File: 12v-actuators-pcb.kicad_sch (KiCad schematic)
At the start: 46 parts, among them J1 EV_1, J10 690367280676, J11 3.5mm WR-TBL, J2 EV_2, J3 EV_3, J4 PURGE, J5 MOTOR_15_1, J6 MOTOR_15_2, J7 MOTOR_15_3, J8 MOTOR_35_1, J9 MOTOR_35_2, Q1 SUM110P06-08L, Q2 2N7002, Q3 2N7002, Q4 G2302, Q5 G2302, Q6 G2302, Q7 G2302, U1 NUCLEO-F042K6, U2 WSEN-PDUS, X1 ESC_Emax_Bullet_15A, X2 ESC_Emax_Bullet_15A, X3 ESC_Emax_Bullet_15A, X4 ESC_Emax_Bullet_35A, X5 ESC_Emax_Bullet_35A

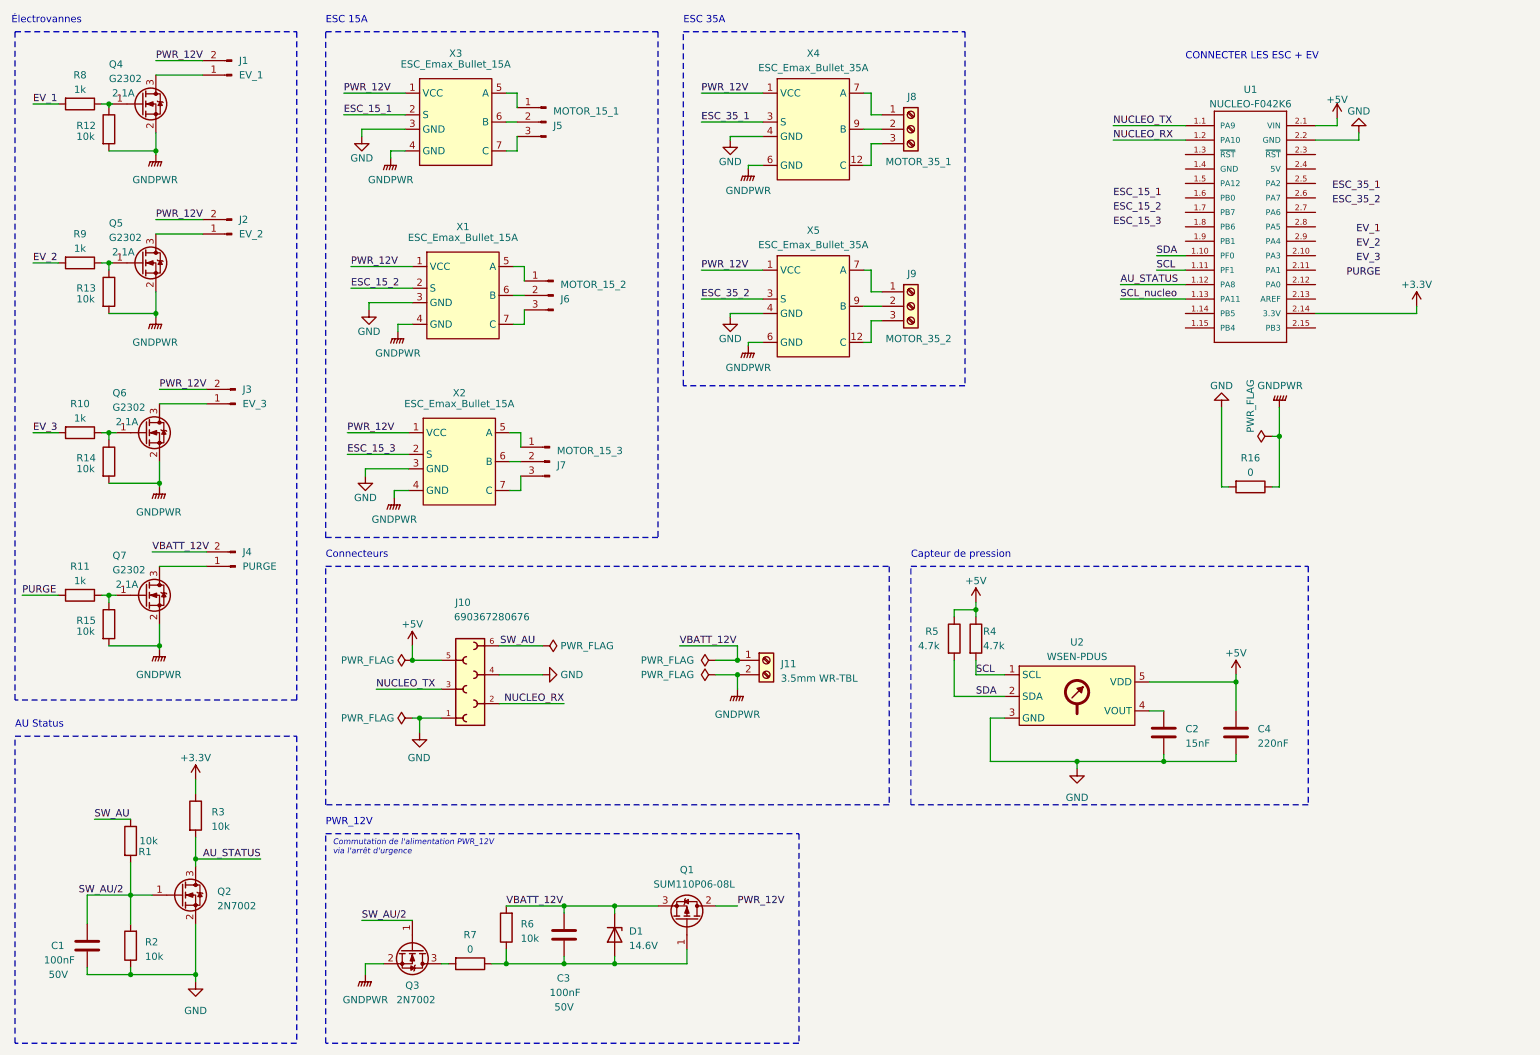
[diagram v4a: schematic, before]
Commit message: Reorganize and finish schematic, assign footprints
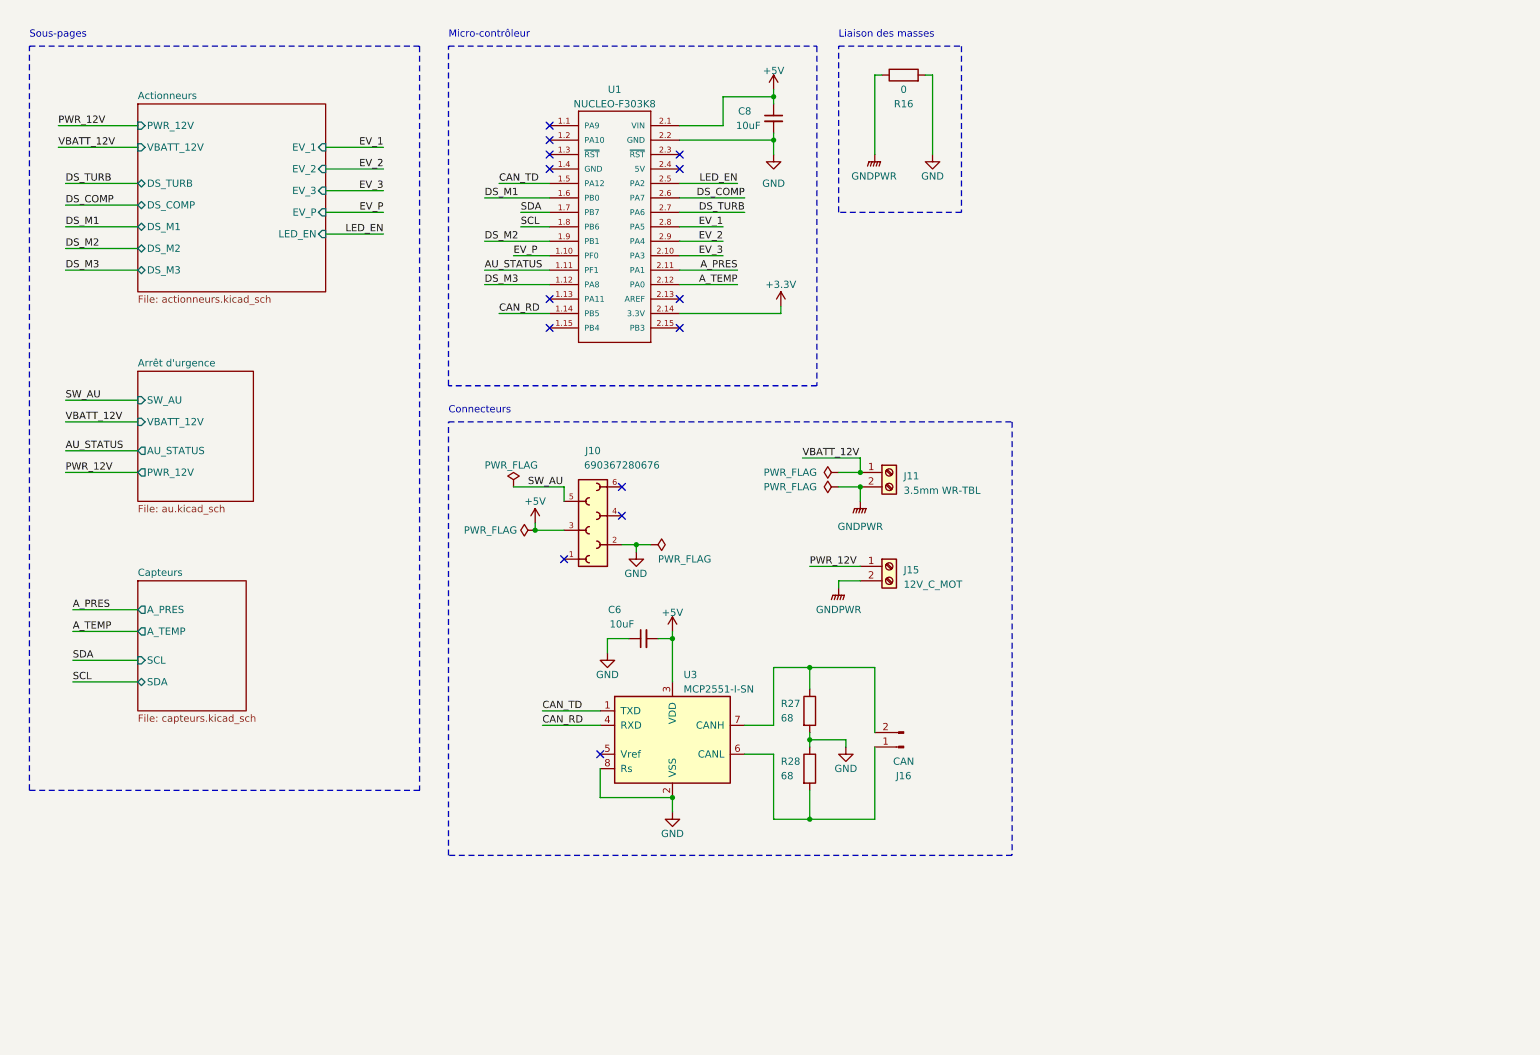
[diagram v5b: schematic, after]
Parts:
- removed C1, C3: 100nF, symbol Device:C
- removed C2: 15nF, symbol Device:C
- removed C4: 220nF, symbol Device:C
- removed D1: 14.6V, symbol Device:D_Zener
- removed J1: EV_1, symbol Connector:Conn_01x02_Pin
- removed J2: EV_2, symbol Connector:Conn_01x02_Pin
- removed J3: EV_3, symbol Connector:Conn_01x02_Pin
- removed J4: PURGE, symbol Connector:Conn_01x02_Pin
- removed J5: MOTOR_15_1, symbol Connector:Conn_01x03_Pin
- removed J6: MOTOR_15_2, symbol Connector:Conn_01x03_Pin
- removed J7: MOTOR_15_3, symbol Connector:Conn_01x03_Pin
- removed J8: MOTOR_35_1, symbol Connector:Screw_Terminal_01x03
- removed J9: MOTOR_35_2, symbol Connector:Screw_Terminal_01x03
- removed Q1: SUM110P06-08L, Package_TO_SOT_SMD:TO-252-2, symbol Transistor_FET:QM6015D
- removed Q2, Q3: 2N7002, Package_TO_SOT_SMD:SOT-23, symbol Transistor_FET:2N7002
- removed Q4, Q5, Q6, Q7: G2302, symbol Device:Q_NMOS_GSD
- removed R1, R2, R3, R6: 10k, Resistor_SMD:R_0201_0603Metric, symbol Device:R
- removed R10, R11, R8, R9: 1k, symbol Device:R
- removed R12, R13, R14, R15: 10k, symbol Device:R
- removed R4, R5: 4.7k, symbol Device:R
- removed R7: 0, Resistor_SMD:R_0201_0603Metric, symbol Device:R
- removed U2: WSEN-PDUS, symbol ComponentsEvo:WSEN-PDUS
- removed X1, X2, X3: ESC_Emax_Bullet_15A, ComponentsEvo:ESC_Emax_Bullet_15A, symbol ComponentsEvo:ESC_Emax_Bullet_15A
- removed X4, X5: ESC_Emax_Bullet_35A, ComponentsEvo:ESC_Emax_Bullet_35A, symbol ComponentsEvo:ESC_Emax_Bullet_35A
- added C6, C8: 10uF, Capacitor_SMD:C_0805_2012Metric, symbol Device:C_Small
- added J15: 12V_C_MOT, ConnectorsEvo:691321100002, symbol Connector:Screw_Terminal_01x02
- added J16: CAN, Connector_PinHeader_2.54mm:PinHeader_1x02_P2.54mm_Vertical, symbol Connector:Conn_01x02_Pin
- added R27, R28: 68, Resistor_SMD:R_0603_1608Metric, symbol Device:R
- added U3: MCP2551-I-SN, Package_SO:SOIC-8_3.9x4.9mm_P1.27mm, symbol Interface_CAN_LIN:MCP2551-I-SN
- J11: footprint (none) -> ConnectorsEvo:691321100002
- R16: footprint (none) -> Resistor_SMD:R_0805_2012Metric
- U1: value NUCLEO-F042K6 -> NUCLEO-F303K8
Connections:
- net +5V: now also J10.3, C6.2, C8.1, U3.3 (VDD); no longer J10.5
- net AU_STATUS: now also U1.1.11 (PF1); no longer U1.1.12 (PA8)
- net EV_1: now also U1.2.8 (PA5)
- net EV_2: now also U1.2.9 (PA4)
- net EV_3: now also U1.2.10 (PA3)
- net GND: now also J10.2, C6.1, C8.2, R27.2, R28.1, U3.2 (VSS), U3.8 (Rs); no longer J10.1, J10.4, J11.2 (Pin_2), R16.1
- net SCL: now also U1.1.8 (PB6); no longer U1.1.11 (PF1)
- net SDA: now also U1.1.7 (PB7); no longer U1.1.10 (PF0)
- net SW_AU: now also J10.5; no longer J10.6
- net CAN_RD: now reaches U1.1.14 (PB5)
- net CAN_RD: now also U3.4 (RXD)
- net CAN_TD: now reaches U1.1.5 (PA12)
- net CAN_TD: now also U3.1 (TXD)
- net DS_M1: now reaches U1.1.6 (PB0)
- net DS_M2: now reaches U1.1.9 (PB1)
- net A_PRES: now reaches U1.2.11 (PA1)
- net A_TEMP: now reaches U1.2.12 (PA0)
- net LED_EN: now reaches U1.2.5 (PA2)
- net DS_COMP: now reaches U1.2.6 (PA7)
- net DS_TURB: now reaches U1.2.7 (PA6)
- net NUCLEO_RX: no longer names the net of U1.1.2 (PA10)
- net NUCLEO_RX: no longer J10.2
- net NUCLEO_TX: no longer names the net of U1.1.1 (PA9)
- net NUCLEO_TX: no longer J10.3
- net SCL_nucleo: no longer names the net of U1.1.13 (PA11)
- new net: J16.1 (Pin_1), R28.2, U3.6 (CANL)
- new net: J16.2 (Pin_2), R27.1, U3.7 (CANH)
- new net DS_M3: U1.1.12 (PA8)
- new net EV_P: U1.1.10 (PF0)
- new net GNDPWR: J11.2 (Pin_2), J15.2 (Pin_2), R16.1
- new net PWR_12V: J15.1 (Pin_1)
- no-connect marks 0 -> 14
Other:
- added sheet Actionneurs (actionneurs.kicad_sch)
- added sheet Arrêt d'urgence (au.kicad_sch)
- added sheet Capteurs (capteurs.kicad_sch)
- note added: "Liaison des masses"
- note added: "Micro-contrôleur"
- note added: "Sous-pages"
- note removed: "AU Status"
- note removed: "CONNECTER LES ESC + EV"
- note removed: "Capteur de pression"
- note removed: "Commutation de l'alimentation PWR_12V via l'arrêt d'urgence"
- note removed: "ESC 15A"
- note removed: "ESC 35A"
- note removed: "PWR_12V"
- note removed: "Électrovannes"
- moved on the sheet: J10, J11, R16, U1

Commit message: Correct CAN interface, add some filtering on sensors + add LCD board power connector
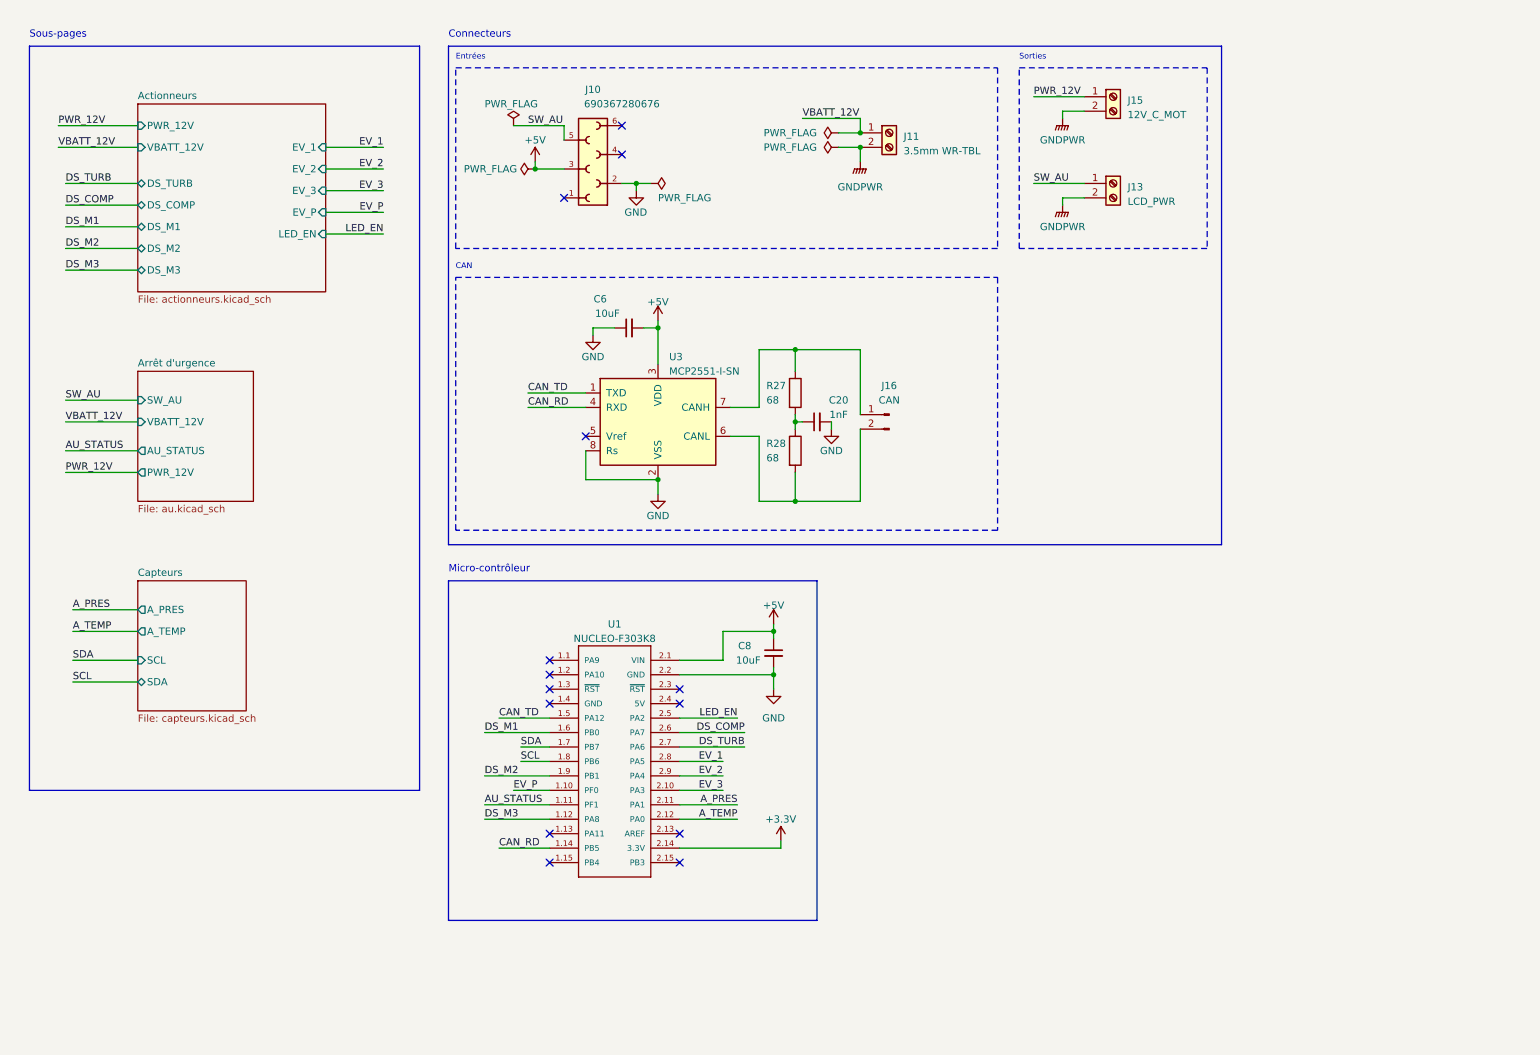
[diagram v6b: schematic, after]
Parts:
- removed R16: 0, Resistor_SMD:R_0805_2012Metric, symbol Device:R
- added C20: 1nF, Capacitor_SMD:C_0805_2012Metric, symbol Device:C_Small
- added J13: LCD_PWR, ConnectorsEvo:691321100002, symbol Connector:Screw_Terminal_01x02
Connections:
- net GND: now also C20.2; no longer R27.2, R28.1
- net GNDPWR: now also J13.2 (Pin_2)
- net SW_AU: now also J13.1 (Pin_1)
- net at R28.2, U3.6 (CANL): now also J16.2 (Pin_2); no longer J16.1 (Pin_1)
- net at R27.1, U3.7 (CANH): now also J16.1 (Pin_1); no longer J16.2 (Pin_2)
- new net: C20.1, R27.2, R28.1
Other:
- note added: "CAN"
- note added: "Entrées"
- note added: "Sorties"
- note removed: "Liaison des masses"
- moved on the sheet: C6, C8, J10, J11, J15, J16, R27, R28, U1, U3

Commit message: Few details -> add filtering on 35A ESC signals + 3.3V capa ...
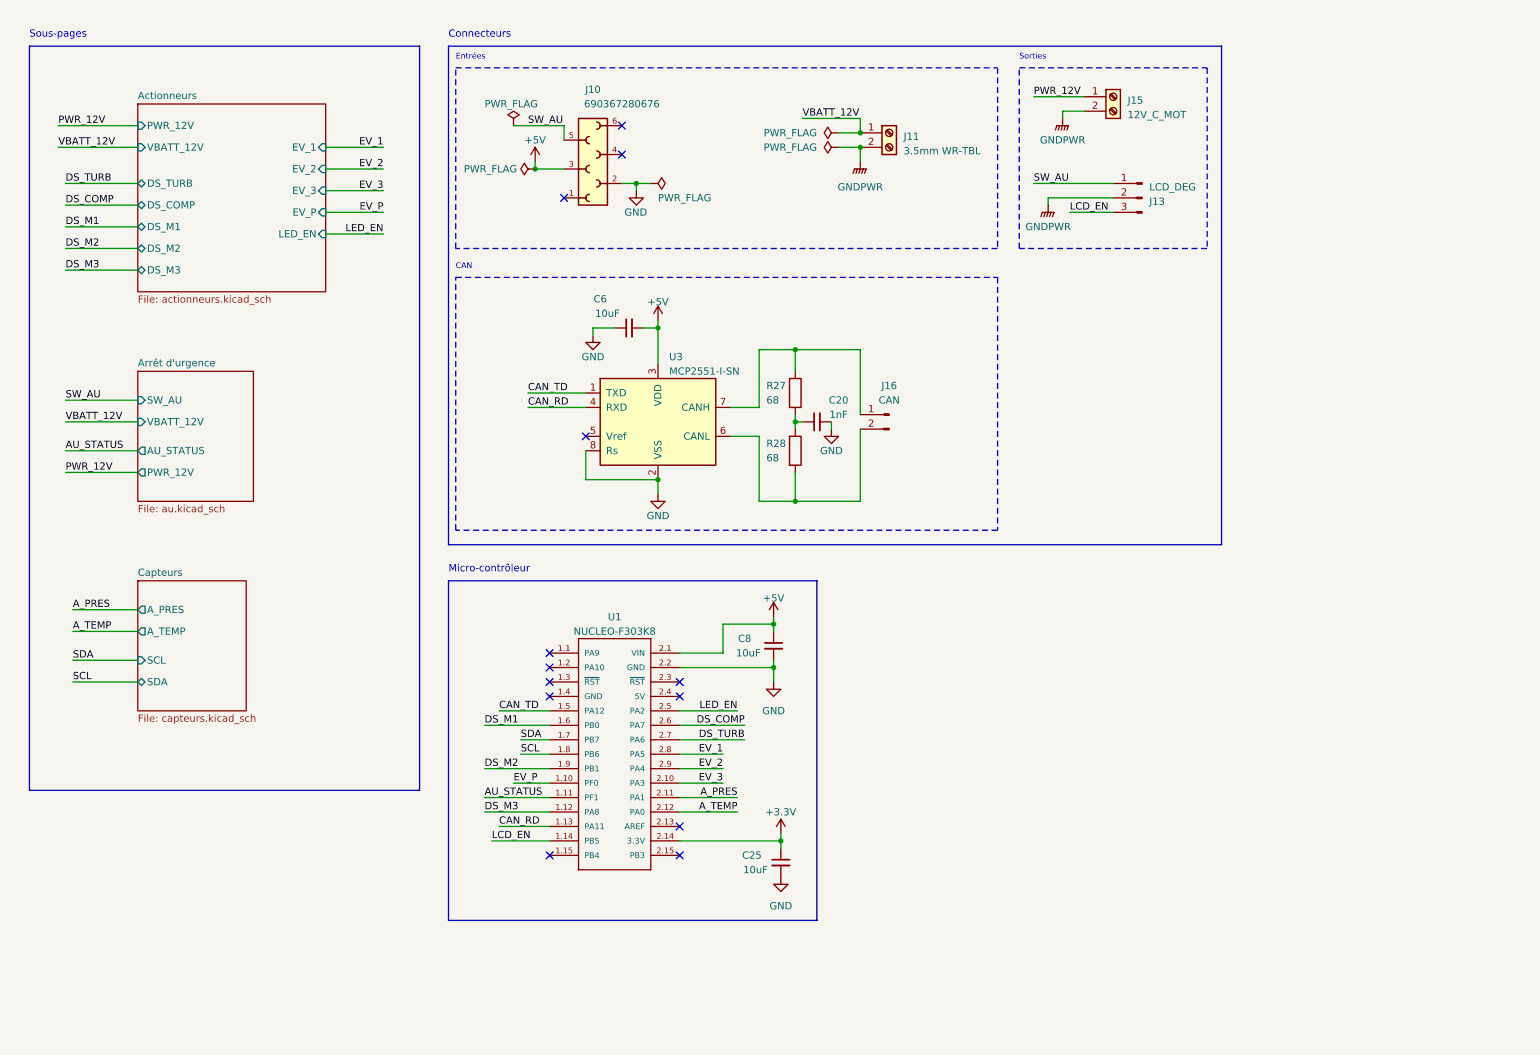
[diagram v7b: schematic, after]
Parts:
- removed J13: LCD_PWR, ConnectorsEvo:691321100002, symbol Connector:Screw_Terminal_01x02
- added C25: 10uF, Capacitor_SMD:C_0805_2012Metric, symbol Device:C_Small
- added J13: LCD_DEG, Connector_PinHeader_2.54mm:PinHeader_1x03_P2.54mm_Vertical, symbol Connector:Conn_01x03_Pin
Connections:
- net +3.3V: now also C25.1
- net CAN_RD: now also U1.1.13 (PA11); no longer U1.1.14 (PB5)
- net GND: now also C25.2
- net GNDPWR: now also J13.2 (Pin_2)
- net SW_AU: now also J13.1 (Pin_1)
- new net LCD_EN: J13.3 (Pin_3), U1.1.14 (PB5)
- no-connect marks 14 -> 13
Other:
- moved on the sheet: C8, U1

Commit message: Schematics finished, reanotated sch
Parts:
- C2: renamed from C20; footprint Capacitor_SMD:C_0805_2012Metric -> Capacitor_SMD:C_0603_1608Metric
- J3: renamed from J10; symbol ComponentsEvo:690367280676 -> ConnectorsEvo:690367280676
- renumbered C6 to C1, C8 to C3, C25 to C4, J15 to J1, J11 to J2, J13 to J4, J16 to J5, R27 to R1, R28 to R2, U3 to U1, U1 to U2
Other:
- note added: "Connecteurs principaux"
- note removed: "Connecteurs"
